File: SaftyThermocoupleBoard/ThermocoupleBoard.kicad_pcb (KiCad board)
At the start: 4 copper layers, 62.6 x 50.4 mm, 62 parts, among them J2 1935161, J3 1935161, J4 1935161, J5 Conn_01x20_Pin, U1 LT1962-3.3, U2 MAX31856, U3 MAX31856, U4 MAX31856

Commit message: add single thermocouple board
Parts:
- removed C12, C14, C15, C20, C22, C23: 0.01uf, Capacitor_SMD:C_0402_1005Metric
- removed C13, C17, C19, C21, C25, C27: 0.1uf, Capacitor_SMD:C_0402_1005Metric
- removed C16, C18, C24, C26: 2.2uF, Capacitor_SMD:C_1206_3216Metric
- removed D2, D3: NUP2105L, Package_TO_SOT_SMD:SOT-23
- removed FB10, FB11, FB12, FB5, FB6, FB7, FB8, FB9: 1.8k, Inductor_SMD:L_0402_1005Metric_Pad0.77x0.64mm_HandSolder
- removed J3, J4: 1935161, SamacSys_Parts:1935161
- removed J5: Conn_01x20_Pin, Connector_PinHeader_2.54mm:PinHeader_1x20_P2.54mm_Horizontal
- removed R10, R11, R6, R7, R8, R9: 2.2k, Resistor_SMD:R_0402_1005Metric
- removed U3, U4: MAX31856, Package_SO:TSSOP-14_4.4x5mm_P0.65mm
- added J1: Conn_02x06_Odd_Even, Connector_PinHeader_2.54mm:PinHeader_2x06_P2.54mm_Horizontal, F.Cu at (94.2, 110.3)
- moved C3 14.7 mm to (86.1, 120.4)
- moved R2 14.7 mm to (82.1, 117.7)
- moved C1 14.7 mm to (79.3, 124.5)
- moved C2 14.7 mm to (83.5, 120.6)
- moved C28 14.7 mm to (82.3, 124.5)
- moved R1 14.7 mm to (83.5, 118.3)
- moved U1 14.7 mm to (79.3, 120.6)
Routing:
- net /thermoDrdy_1: track 47.5 -> 0.00 mm, vias 1 -> 0
- net /MOSI: track 59.4 -> 12.0 mm, vias 2 -> 0
- net /MISO: track 58.5 -> 13.7 mm, vias 4 -> 0
- net /CLK: track 59.8 -> 15.1 mm, vias 2 -> 0
- net /CS2: track 39.6 -> 0.00 mm, vias 2 -> 0
- net /thermoFault_1: track 37.7 -> 0.00 mm, vias 1 -> 0
- net /thermoFault_0: track 44.0 -> 10.1 mm, vias 2 -> 0
- net 3.3V_A: track 59.4 -> 29.1 mm, vias 5 -> 1
- net /thermoDrdy_2: track 29.0 -> 0.00 mm, vias 2 -> 0
- net 3.3_D: track 57.5 -> 29.8 mm, vias 6 -> 4
- net /thermoDrdy_0: track 43.2 -> 17.4 mm
- net /thermoFault_2: track 25.2 -> 0.00 mm
- net /CS1: track 24.3 -> 0.00 mm, vias 2 -> 0
- net GND: track 46.4 -> 24.9 mm, vias 21 -> 9
- net 5V: track 19.8 -> 33.9 mm
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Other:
- board size 62.6 x 50.4 mm -> 37.9 x 39.3 mm

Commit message: progress
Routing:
- net 3.3V_A: track 29.1 -> 20.4 mm, vias 1 -> 0
- net Net-(U2-DVDD): track 10.2 -> 17.4 mm, vias 1 -> 3
- net 3.3_D: track 29.8 -> 24.4 mm, vias 4 -> 2
- net GND: track 24.9 -> 28.5 mm, vias 9 -> 35
- removed copper zone on In1.Cu, net GND
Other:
- copper layers 4 -> 2

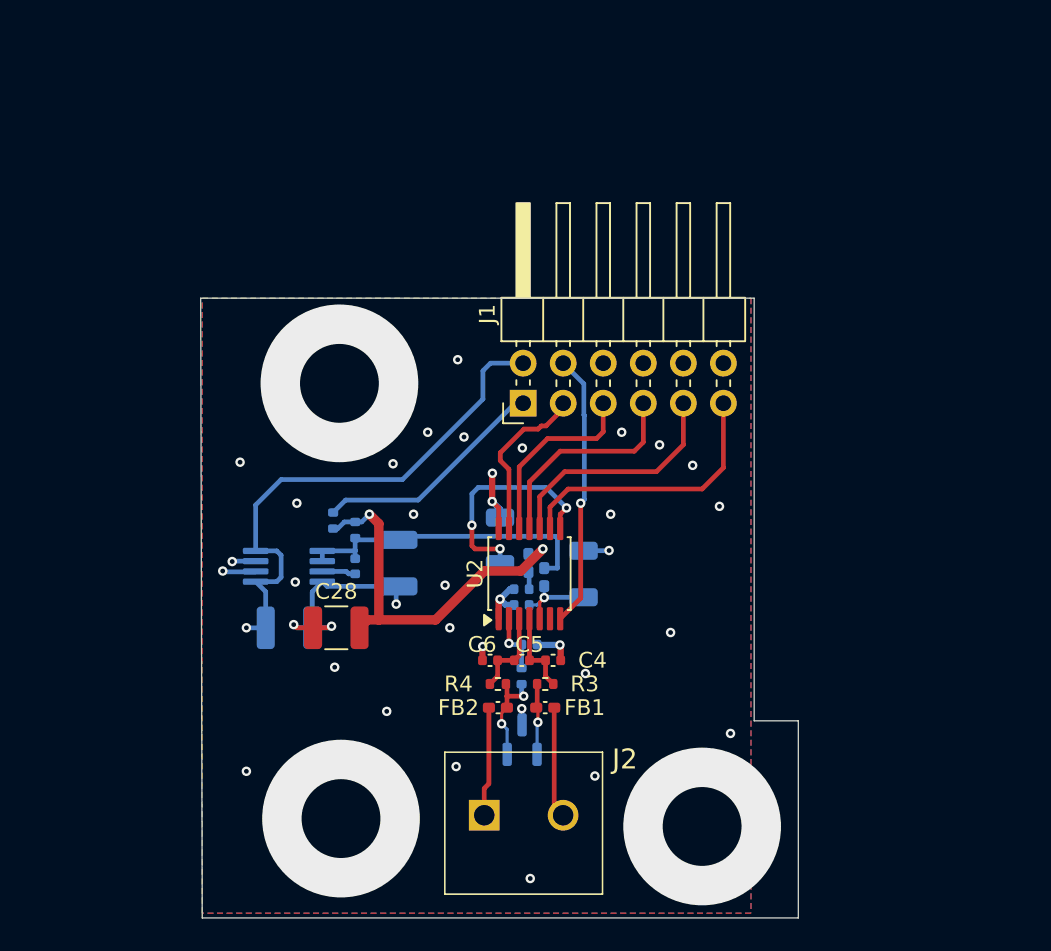
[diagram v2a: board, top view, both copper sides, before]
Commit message: add a unit test fixture, and start changing the current measurement circuit
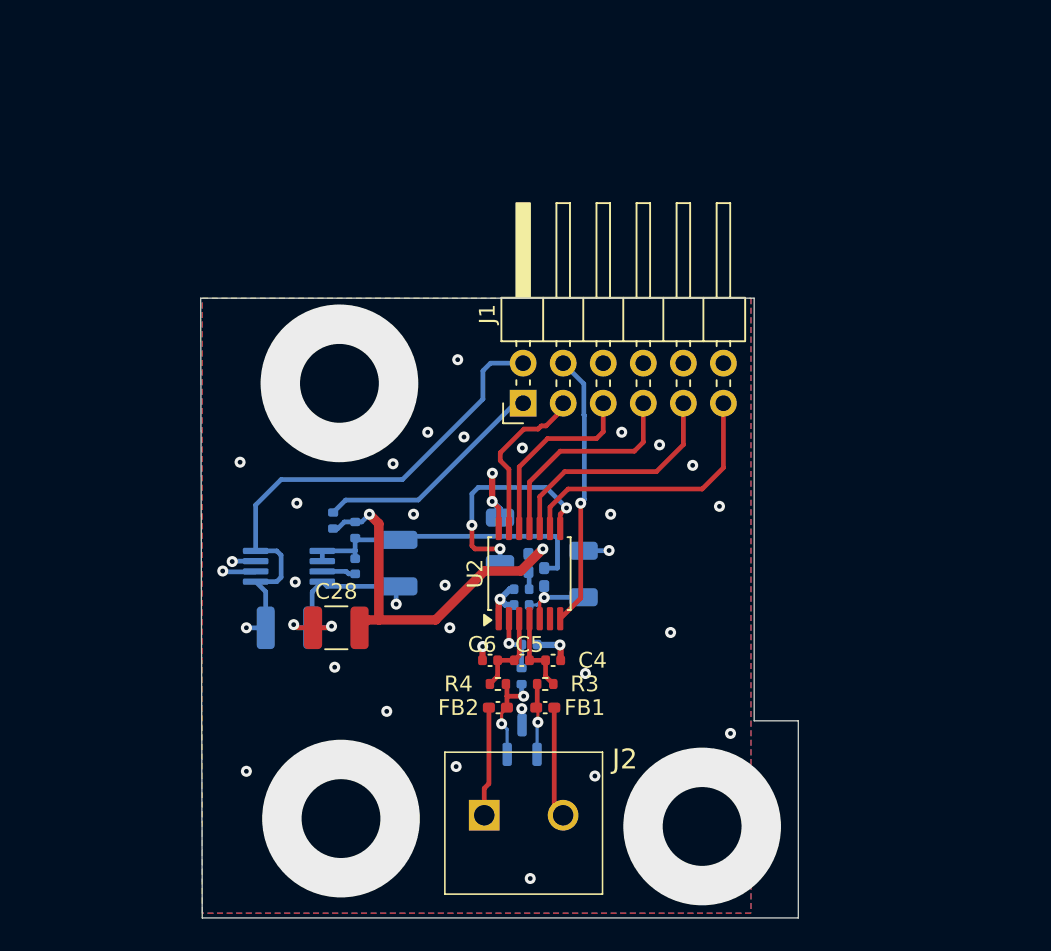
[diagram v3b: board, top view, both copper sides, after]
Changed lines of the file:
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@@
 			(plot_on_all_layers_selection 0x00000000_00000000_00000000_00000000)
 			(disableapertmacros no)
-			(usegerberextensions no)
-			(usegerberattributes yes)
-			(usegerberadvancedattributes yes)
+			(usegerberextensions yes)
+			(usegerberattributes no)
+			(usegerberadvancedattributes no)
 			(creategerberjobfile yes)
 			(dashed_line_dash_ratio 12)
@@
 			(sketchdnponfab yes)
 			(crossoutdnponfab yes)
-			(subtractmaskfromsilk no)
+			(subtractmaskfromsilk yes)
 			(outputformat 1)
 			(mirror no)
-			(drillshape 1)
+			(drillshape 0)
 			(scaleselection 1)
-			(outputdirectory "")
+			(outputdirectory "output")
 		)
 	)
@@
 	(via
 		(at 76.6 124.5)
-		(size 0.6)
+		(size 0.7)
 		(drill 0.3)
 		(layers "F.Cu" "B.Cu")
@@
 	(via
 		(at 97.8 116.6)
-		(size 0.6)
+		(size 0.7)
 		(drill 0.3)
 		(layers "F.Cu" "B.Cu")
@@
 	(via
 		(at 88.1 112.1)
-		(size 0.6)
+		(size 0.7)
 		(drill 0.3)
 		(layers "F.Cu" "B.Cu")
@@
 	(via
 		(at 79.7 121.6)
-		(size 0.6)
+		(size 0.7)
 		(drill 0.3)
 		(layers "F.Cu" "B.Cu")
@@
 	(via
 		(at 89.9 133.3)
-		(size 0.6)
+		(size 0.7)
 		(drill 0.3)
 		(layers "F.Cu" "B.Cu")
@@
 	(via
 		(at 94.062953 129.629357)
-		(size 0.6)
+		(size 0.7)
 		(drill 0.3)
 		(layers "F.Cu" "B.Cu")
@@
 	(via
 		(at 79.8 116.6)
-		(size 0.6)
+		(size 0.7)
 		(drill 0.3)
 		(layers "F.Cu" "B.Cu")
@@
 	(via
 		(at 89.5 124.5)
-		(size 0.6)
+		(size 0.7)
 		(drill 0.3)
 		(layers "F.Cu" "B.Cu")
@@
 	(via
 		(at 86.1 123)
-		(size 0.6)
+		(size 0.7)
 		(drill 0.3)
 		(layers "F.Cu" "B.Cu")
@@
 	(via
 		(at 76.2 114)
-		(size 0.6)
+		(size 0.7)
 		(drill 0.3)
 		(layers "F.Cu" "B.Cu")
@@
 	(via
 		(at 87.2 117.3)
-		(size 0.6)
+		(size 0.7)
 		(drill 0.3)
 		(layers "F.Cu" "B.Cu")
@@
 	(via
 		(at 94.6 140.4)
-		(size 0.6)
+		(size 0.7)
 		(drill 0.3)
 		(layers "F.Cu" "B.Cu")
@@
 	(via
 		(at 82.2 127)
-		(size 0.6)
+		(size 0.7)
 		(drill 0.3)
 		(layers "F.Cu" "B.Cu")
@@
 	(via
 		(at 92.684599 122.688657)
-		(size 0.6)
+		(size 0.7)
 		(drill 0.3)
 		(layers "F.Cu" "B.Cu")
@@
 	(via
 		(at 85.9 114.1)
-		(size 0.6)
+		(size 0.7)
 		(drill 0.3)
 		(layers "F.Cu" "B.Cu")
@@
 	(via
 		(at 82 124.4)
-		(size 0.6)
+		(size 0.7)
 		(drill 0.3)
 		(layers "F.Cu" "B.Cu")
@@
 	(via
 		(at 98.7 133.9)
-		(size 0.6)
+		(size 0.7)
 		(drill 0.3)
 		(layers "F.Cu" "B.Cu")
@@
 	(via
 		(at 100.4 112.1)
-		(size 0.6)
+		(size 0.7)
 		(drill 0.3)
 		(layers "F.Cu" "B.Cu")
@@
 	(via
 		(at 103.5 124.8)
-		(size 0.6)
+		(size 0.7)
 		(drill 0.3)
 		(layers "F.Cu" "B.Cu")
@@
 	(via
 		(at 96.484599 125.588657)
-		(size 0.6)
+		(size 0.7)
 		(drill 0.3)
 		(layers "F.Cu" "B.Cu")
@@
 	(via
 		(at 91.584599 125.688657)
-		(size 0.6)
+		(size 0.7)
 		(drill 0.3)
 		(layers "F.Cu" "B.Cu")
@@
 	(via
 		(at 106.6 116.8)
-		(size 0.6)
+		(size 0.7)
 		(drill 0.3)
 		(layers "F.Cu" "B.Cu")
@@
 	(via
 		(at 90.4 112.4)
-		(size 0.6)
+		(size 0.7)
 		(drill 0.3)
 		(layers "F.Cu" "B.Cu")
@@
 	(via
 		(at 94.1 113.1)
-		(size 0.6)
+		(size 0.7)
 		(drill 0.3)
 		(layers "F.Cu" "B.Cu")
@@
 	(via
 		(at 85.5 129.8)
-		(size 0.6)
+		(size 0.7)
 		(drill 0.3)
 		(layers "F.Cu" "B.Cu")
@@
 	(via
 		(at 92.184599 116.488657)
-		(size 0.6)
+		(size 0.7)
 		(drill 0.3)
 		(layers "F.Cu" "B.Cu")
@@
 	(via
 		(at 104.9 114.2)
-		(size 0.6)
+		(size 0.7)
 		(drill 0.3)
 		(layers "F.Cu" "B.Cu")
@@
 	(via
 		(at 99.7 117.3)
-		(size 0.6)
+		(size 0.7)
 		(drill 0.3)
 		(layers "F.Cu" "B.Cu")
@@
 	(via
 		(at 102.8 112.9)
-		(size 0.6)
+		(size 0.7)
 		(drill 0.3)
 		(layers "F.Cu" "B.Cu")
@@
 	(via
 		(at 89.2 121.8)
-		(size 0.6)
+		(size 0.7)
 		(drill 0.3)
 		(layers "F.Cu" "B.Cu")
@@
 	(via
 		(at 90 107.5)
-		(size 0.6)
+		(size 0.7)
 		(drill 0.3)
 		(layers "F.Cu" "B.Cu")
@@
 	(via
 		(at 79.6 124.3)
-		(size 0.6)
+		(size 0.7)
 		(drill 0.3)
 		(layers "F.Cu" "B.Cu")
@@
 	(via
 		(at 107.3 131.2)
-		(size 0.6)
+		(size 0.7)
 		(drill 0.3)
 		(layers "F.Cu" "B.Cu")
@@
 	(via
 		(at 76.6 133.6)
-		(size 0.6)
+		(size 0.7)
 		(drill 0.3)
 		(layers "F.Cu" "B.Cu")
@@
 	(via
 		(at 92.2 114.7)
-		(size 0.6)
+		(size 0.7)
 		(drill 0.3)
 		(layers "F.Cu" "B.Cu")
@@
 	(via
 		(at 98.1 127.4)
-		(size 0.6)
+		(size 0.7)
 		(drill 0.3)
 		(layers "F.Cu" "B.Cu")
@@
 	(via
 		(at 99.6 119.6)
-		(size 0.6)
+		(size 0.7)
 		(drill 0.3)
 		(layers "F.Cu" "B.Cu")
@@
 	(via
 		(at 84.4 117.3)
-		(size 0.6)
+		(size 0.7)
 		(drill 0.3)
 		(layers "F.Cu" "B.Cu")
@@
 	(via
 		(at 95.4 119.5)
-		(size 0.6)
+		(size 0.7)
 		(drill 0.3)
 		(layers "F.Cu" "B.Cu")
@@
 	(via
 		(at 95.084599 130.488657)
-		(size 0.6)
+		(size 0.7)
 		(drill 0.3)
 		(layers "F.Cu" "B.Cu")
@@
 	(via
 		(at 93.25 125.488657)
-		(size 0.6)
+		(size 0.7)
 		(drill 0.3)
 		(layers "F.Cu" "B.Cu")
@@
 	(via
 		(at 95.484599 122.588657)
-		(size 0.6)
+		(size 0.7)
 		(drill 0.3)
 		(layers "F.Cu" "B.Cu")
@@
 	(via
 		(at 92.684599 119.488657)
-		(size 0.6)
+		(size 0.7)
 		(drill 0.3)
 		(layers "F.Cu" "B.Cu")
@@
 	(via
 		(at 96.9 116.9)
-		(size 0.6)
+		(size 0.7)
 		(drill 0.3)
 		(layers "F.Cu" "B.Cu")
@@
 	(via
 		(at 90.9 118)
-		(size 0.6)
+		(size 0.7)
 		(drill 0.3)
 		(layers "F.Cu" "B.Cu")
@@
 	(via
 		(at 92.784599 130.588657)
-		(size 0.6)
+		(size 0.7)
 		(drill 0.3)
 		(layers "F.Cu" "B.Cu")
@@
 	(via
 		(at 94.184599 128.838657)
-		(size 0.6)
+		(size 0.7)
 		(drill 0.3)
 		(layers "F.Cu" "B.Cu")
@@
 	(via
 		(at 75.1 120.9)
-		(size 0.6)
+		(size 0.7)
 		(drill 0.3)
 		(layers "F.Cu" "B.Cu")
@@
 	(via
 		(at 75.7 120.3)
-		(size 0.6)
+		(size 0.7)
 		(drill 0.3)
 		(layers "F.Cu" "B.Cu")

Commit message: mainboard pcb changes for jlc pcb dfm
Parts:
- J1: footprint Connector_PinHeader_2.54mm:PinHeader_2x06_P2.54mm_Horizontal -> Connector_PinHeader_1.27mm:PinHeader_2x06_P1.27mm_Horizontal
- moved J1 3.67 mm to (97.3, 108.5)

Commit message: safty tc board changes
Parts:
- moved J1 2.98 mm to (99.7, 106.6)
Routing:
- net /thermoDrdy_0: track 17.4 -> 25.8 mm, vias 1 -> 2
- net Net-(J1-Pin_1): track 14.9 -> 21.9 mm, vias 0 -> 1
- net /thermoFault_0: track 10.5 -> 16.5 mm
- net 5V: track 33.9 -> 39.6 mm
- net /MOSI: track 12.0 -> 16.9 mm
- net /MISO: track 13.7 -> 18.1 mm
- net /CS0: track 17.5 -> 21.5 mm
- net /CLK: track 15.1 -> 19.0 mm
- net GND: track 28.5 -> 31.2 mm, vias 35 -> 42
- net Net-(U2-BIAS): track 3.91 -> 4.50 mm
